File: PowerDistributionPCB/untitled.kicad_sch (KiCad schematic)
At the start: 1 part

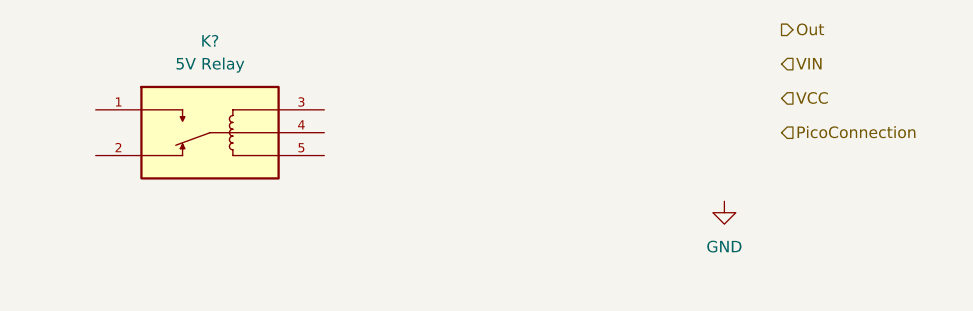
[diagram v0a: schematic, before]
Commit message: added relay connections
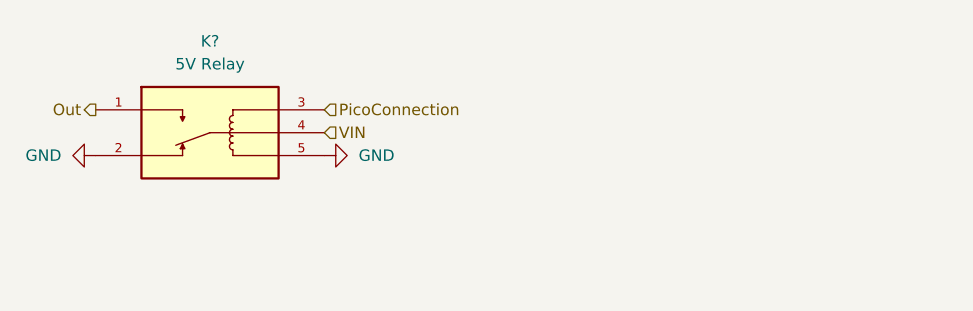
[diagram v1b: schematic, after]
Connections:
- net GND: now also K?.2, K?.5
- net Out: now also K?.1
- net PicoConnection: now also K?.3
- net VIN: now also K?.4
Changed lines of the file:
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@@
 	(hierarchical_label "PicoConnection"
 		(shape input)
-		(at 184.15 62.23 0)
+		(at 133.35 59.69 0)
 		(effects
 			(font
@@
 	(hierarchical_label "VIN"
 		(shape input)
-		(at 184.15 54.61 0)
+		(at 133.35 62.23 0)
 		(effects
 			(font
@@
 		)
 	)
-	(hierarchical_label "VCC"
-		(shape input)
-		(at 184.15 58.42 0)
+	(hierarchical_label "Out"
+		(shape output)
+		(at 107.95 59.69 180)
 		(effects
 			(font
 				(size 1.27 1.27)
 			)
-			(justify left)
-		)
-	)
-	(hierarchical_label "Out"
-		(shape output)
-		(at 184.15 50.8 0)
-		(effects
-			(font
-				(size 1.27 1.27)
-			)
-			(justify left)
+			(justify right)
 		)
 	)
@@
 		)
 		(instances
-			(project ""
+			(project "PowerDistributionPCB"
+				(path "/b27c75df-6223-4cc6-be69-062c2b02d5c6/4aa10ec7-4b36-4cde-a760-c4500e70a751"
+					(reference "K?")
+					(unit 1)
+				)
 				(path "/b27c75df-6223-4cc6-be69-062c2b02d5c6/bfd015dc-a1f5-42ba-b972-f7703fed8888"
 					(reference "K?")
@@
 	(symbol
 		(lib_id "power:GND")
-		(at 177.8 69.85 0)
+		(at 107.95 64.77 270)
+		(unit 1)
+		(exclude_from_sim no)
+		(in_bom yes)
+		(on_board yes)
+		(dnp no)
+		(fields_autoplaced yes)
+		(property "Reference" "#PWR013"
+			(at 101.6 64.77 0)
+			(effects
+				(font
+					(size 1.27 1.27)
+				)
+				(hide yes)
+			)
+		)
+		(property "Value" "GND"
+			(at 104.14 64.7699 90)
+			(effects
+				(font
+					(size 1.27 1.27)
+				)
+				(justify right)
+			)
+		)
+		(property "Footprint" ""
+			(at 107.95 64.77 0)
+			(effects
+				(font
+					(size 1.27 1.27)
+				)
+				(hide yes)
+			)
+		)
+		(property "Datasheet" ""
+			(at 107.95 64.77 0)
+			(effects
+				(font
+					(size 1.27 1.27)
+				)
+				(hide yes)
+			)
+		)
+		(property "Description" "Power symbol creates a global label with name \"GND\" , ground"
+			(at 107.95 64.77 0)
+			(effects
+				(font
+					(size 1.27 1.27)
+				)
+				(hide yes)
+			)
+		)
+		(pin "1"
+		)
+		(instances
+			(project "PowerDistributionPCB"
+				(path "/b27c75df-6223-4cc6-be69-062c2b02d5c6/4aa10ec7-4b36-4cde-a760-c4500e70a751"
+					(reference "#PWR014")
+					(unit 1)
+				)
+				(path "/b27c75df-6223-4cc6-be69-062c2b02d5c6/bfd015dc-a1f5-42ba-b972-f7703fed8888"
+					(reference "#PWR013")
+					(unit 1)
+				)
+			)
+		)
+	)
+	(symbol
+		(lib_id "power:GND")
+		(at 133.35 64.77 90)
 		(unit 1)
 		(exclude_from_sim no)
@@
 		(fields_autoplaced yes)
 		(property "Reference" "#PWR?"
-			(at 177.8 76.2 0)
+			(at 139.7 64.77 0)
 			(effects
 				(font
@@
 		)
 		(property "Value" "GND"
-			(at 177.8 74.93 0)
-			(effects
-				(font
-					(size 1.27 1.27)
-				)
+			(at 137.16 64.7699 90)
+			(effects
+				(font
+					(size 1.27 1.27)
+				)
+				(justify right)
 			)
 		)
 		(property "Footprint" ""
-			(at 177.8 69.85 0)
+			(at 133.35 64.77 0)
 			(effects
 				(font
@@
 		)
 		(property "Datasheet" ""
-			(at 177.8 69.85 0)
+			(at 133.35 64.77 0)
 			(effects
 				(font
@@
 		)
 		(property "Description" "Power symbol creates a global label with name \"GND\" , ground"
-			(at 177.8 69.85 0)
-			(effects
-				(font
+			(at 133.35 64.77 0)
+			(effects
+				(font

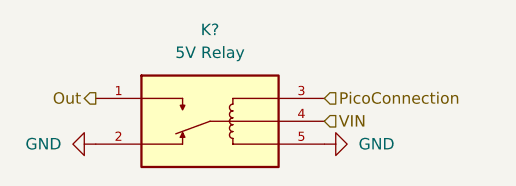
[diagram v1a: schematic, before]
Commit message: switched pico to arduino, started implementing 3.3 relay and updated connections
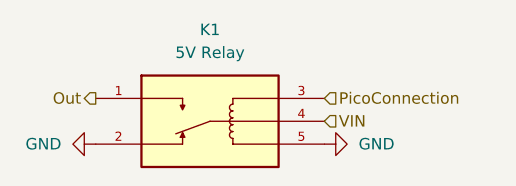
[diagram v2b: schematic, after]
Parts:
- gave numbers to parts that had none: 1
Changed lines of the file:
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@@
 		(dnp no)
 		(fields_autoplaced yes)
-		(property "Reference" "K?"
+		(property "Reference" "K1"
 			(at 120.65 52.07 0)
 			(effects
@@
 		(instances
 			(project "PowerDistributionPCB"
+				(path "/b27c75df-6223-4cc6-be69-062c2b02d5c6/0499fe0a-5226-48d2-93fa-51ba0d86cbfb"
+					(reference "K1")
+					(unit 1)
+				)
 				(path "/b27c75df-6223-4cc6-be69-062c2b02d5c6/4aa10ec7-4b36-4cde-a760-c4500e70a751"
 					(reference "K?")
@@
 		(dnp no)
 		(fields_autoplaced yes)
-		(property "Reference" "#PWR013"
+		(property "Reference" "#PWR016"
 			(at 101.6 64.77 0)
 			(effects
@@
 		(instances
 			(project "PowerDistributionPCB"
+				(path "/b27c75df-6223-4cc6-be69-062c2b02d5c6/0499fe0a-5226-48d2-93fa-51ba0d86cbfb"
+					(reference "#PWR016")
+					(unit 1)
+				)
 				(path "/b27c75df-6223-4cc6-be69-062c2b02d5c6/4aa10ec7-4b36-4cde-a760-c4500e70a751"
 					(reference "#PWR014")
@@
 		(dnp no)
 		(fields_autoplaced yes)
-		(property "Reference" "#PWR?"
+		(property "Reference" "#PWR017"
 			(at 139.7 64.77 0)
 			(effects
@@
 		(instances
 			(project "PowerDistributionPCB"
+				(path "/b27c75df-6223-4cc6-be69-062c2b02d5c6/0499fe0a-5226-48d2-93fa-51ba0d86cbfb"
+					(reference "#PWR017")
+					(unit 1)
+				)
 				(path "/b27c75df-6223-4cc6-be69-062c2b02d5c6/4aa10ec7-4b36-4cde-a760-c4500e70a751"
 					(reference "#PWR01")

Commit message: relay implementation
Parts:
- added D1: 1N4007, Diode_THT:D_DO-41_SOD81_P10.16mm_Horizontal, symbol Diode:1N4007
- added Q1: PN2222A, Package_TO_SOT_THT:TO-92_Inline, symbol Transistor_BJT:PN2222A
- added R1: R, symbol Device:R
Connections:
- net GND: now also Q1.1 (E); no longer K1.2, K1.5
- net Out: now also K1.2; no longer K1.1
- net PicoConnection: now also R1.1; no longer K1.3
- new net: Q1.2 (B), R1.2
- new net: D1.2 (A), K1.5, Q1.3 (C)
- new net 5V: D1.1 (K), K1.3

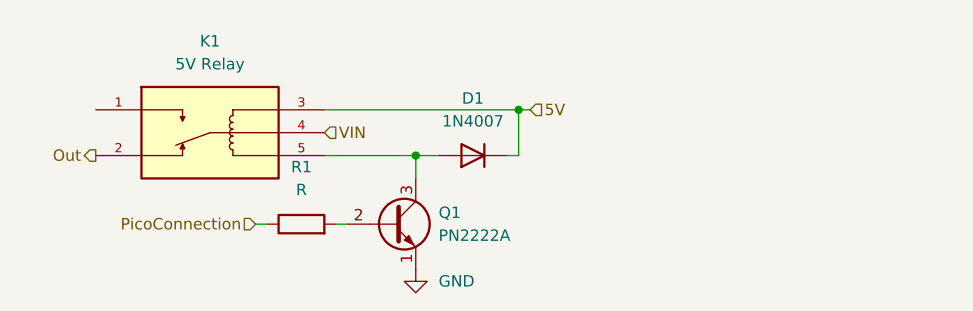
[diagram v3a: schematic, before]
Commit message: started reworking relays for new relay design
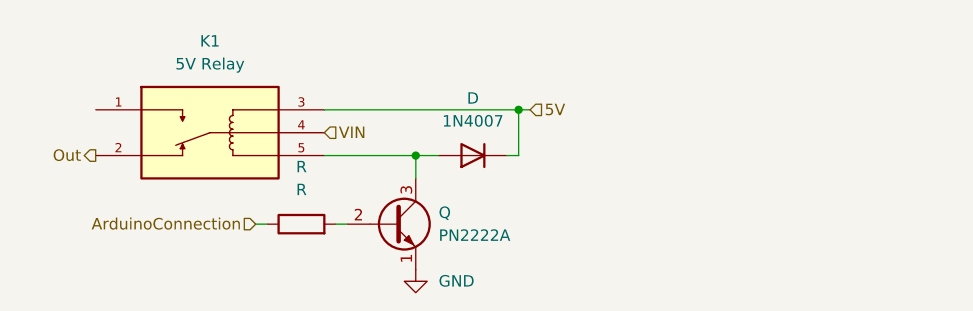
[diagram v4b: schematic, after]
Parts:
- renumbered D1 to D, Q1 to Q, R1 to R
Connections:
- net PicoConnection renamed ArduinoConnection
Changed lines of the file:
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@@
 		)
 	)
-	(hierarchical_label "PicoConnection"
+	(hierarchical_label "ArduinoConnection"
 		(shape input)
 		(at 125.73 72.39 180)
@@
 		(dnp no)
 		(fields_autoplaced yes)
-		(property "Reference" "Q1"
+		(property "Reference" "Q"
 			(at 146.05 71.1199 0)
 			(effects
@@
 		)
 		(instances
-			(project ""
-				(path "/b27c75df-6223-4cc6-be69-062c2b02d5c6/0499fe0a-5226-48d2-93fa-51ba0d86cbfb"
-					(reference "Q1")
-					(unit 1)
-				)
-				(path "/b27c75df-6223-4cc6-be69-062c2b02d5c6/4aa10ec7-4b36-4cde-a760-c4500e70a751"
+			(project "PowerDistributionPCB"
+				(path "/b27c75df-6223-4cc6-be69-062c2b02d5c6/2a69d7e0-98c2-47cd-b7c8-14763472c0d8"
 					(reference "Q3")
 					(unit 1)
 				)
-				(path "/b27c75df-6223-4cc6-be69-062c2b02d5c6/bfd015dc-a1f5-42ba-b972-f7703fed8888"
+				(path "/b27c75df-6223-4cc6-be69-062c2b02d5c6/a2f984ed-c504-464a-8131-e8a4707504b7"
 					(reference "Q2")
+					(unit 1)
+				)
+				(path "/b27c75df-6223-4cc6-be69-062c2b02d5c6/fcb51314-c7c2-4c49-a056-3b722a5b6f6e"
+					(reference "Q4")
 					(unit 1)
 				)
@@
 					(unit 1)
 				)
-				(path "/b27c75df-6223-4cc6-be69-062c2b02d5c6/4aa10ec7-4b36-4cde-a760-c4500e70a751"
-					(reference "K?")
-					(unit 1)
-				)
-				(path "/b27c75df-6223-4cc6-be69-062c2b02d5c6/bfd015dc-a1f5-42ba-b972-f7703fed8888"
-					(reference "K?")
+				(path "/b27c75df-6223-4cc6-be69-062c2b02d5c6/2a69d7e0-98c2-47cd-b7c8-14763472c0d8"
+					(reference "K3")
+					(unit 1)
+				)
+				(path "/b27c75df-6223-4cc6-be69-062c2b02d5c6/a2f984ed-c504-464a-8131-e8a4707504b7"
+					(reference "K2")
+					(unit 1)
+				)
+				(path "/b27c75df-6223-4cc6-be69-062c2b02d5c6/fcb51314-c7c2-4c49-a056-3b722a5b6f6e"
+					(reference "K4")
 					(unit 1)
 				)
@@
 		(dnp no)
 		(fields_autoplaced yes)
-		(property "Reference" "D1"
+		(property "Reference" "D"
 			(at 149.86 58.42 0)
 			(effects
@@
 		)
 		(instances
-			(project ""
-				(path "/b27c75df-6223-4cc6-be69-062c2b02d5c6/0499fe0a-5226-48d2-93fa-51ba0d86cbfb"
-					(reference "D1")
-					(unit 1)
-				)
-				(path "/b27c75df-6223-4cc6-be69-062c2b02d5c6/4aa10ec7-4b36-4cde-a760-c4500e70a751"
+			(project "PowerDistributionPCB"
+				(path "/b27c75df-6223-4cc6-be69-062c2b02d5c6/2a69d7e0-98c2-47cd-b7c8-14763472c0d8"
 					(reference "D3")
 					(unit 1)
 				)
-				(path "/b27c75df-6223-4cc6-be69-062c2b02d5c6/bfd015dc-a1f5-42ba-b972-f7703fed8888"
+				(path "/b27c75df-6223-4cc6-be69-062c2b02d5c6/a2f984ed-c504-464a-8131-e8a4707504b7"
 					(reference "D2")
+					(unit 1)
+				)
+				(path "/b27c75df-6223-4cc6-be69-062c2b02d5c6/fcb51314-c7c2-4c49-a056-3b722a5b6f6e"
+					(reference "D4")
 					(unit 1)
 				)
@@
 					(unit 1)
 				)
-				(path "/b27c75df-6223-4cc6-be69-062c2b02d5c6/4aa10ec7-4b36-4cde-a760-c4500e70a751"
-					(reference "#PWR01")
-					(unit 1)
-				)
-				(path "/b27c75df-6223-4cc6-be69-062c2b02d5c6/bfd015dc-a1f5-42ba-b972-f7703fed8888"
-					(reference "#PWR?")
+				(path "/b27c75df-6223-4cc6-be69-062c2b02d5c6/2a69d7e0-98c2-47cd-b7c8-14763472c0d8"
+					(reference "#PWR014")
+					(unit 1)
+				)
+				(path "/b27c75df-6223-4cc6-be69-062c2b02d5c6/a2f984ed-c504-464a-8131-e8a4707504b7"
+					(reference "#PWR013")
+					(unit 1)
+				)
+				(path "/b27c75df-6223-4cc6-be69-062c2b02d5c6/fcb51314-c7c2-4c49-a056-3b722a5b6f6e"
+					(reference "#PWR022")
 					(unit 1)
 				)
@@
 		(dnp no)
 		(fields_autoplaced yes)
-		(property "Reference" "R1"
+		(property "Reference" "R"
 			(at 130.81 66.04 90)
 			(effects
@@
 		)
 		(instances
-			(project ""
-				(path "/b27c75df-6223-4cc6-be69-062c2b02d5c6/0499fe0a-5226-48d2-93fa-51ba0d86cbfb"
-					(reference "R1")
-					(unit 1)
-				)
-				(path "/b27c75df-6223-4cc6-be69-062c2b02d5c6/4aa10ec7-4b36-4cde-a760-c4500e70a751"
+			(project "PowerDistributionPCB"
+				(path "/b27c75df-6223-4cc6-be69-062c2b02d5c6/2a69d7e0-98c2-47cd-b7c8-14763472c0d8"
 					(reference "R3")
 					(unit 1)
 				)
-				(path "/b27c75df-6223-4cc6-be69-062c2b02d5c6/bfd015dc-a1f5-42ba-b972-f7703fed8888"
+				(path "/b27c75df-6223-4cc6-be69-062c2b02d5c6/a2f984ed-c504-464a-8131-e8a4707504b7"
 					(reference "R2")
 					(unit 1)
 				)
+				(path "/b27c75df-6223-4cc6-be69-062c2b02d5c6/fcb51314-c7c2-4c49-a056-3b722a5b6f6e"
+					(reference "R4")
+					(unit 1)
+				)
